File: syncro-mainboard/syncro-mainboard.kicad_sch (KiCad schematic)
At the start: 0 parts

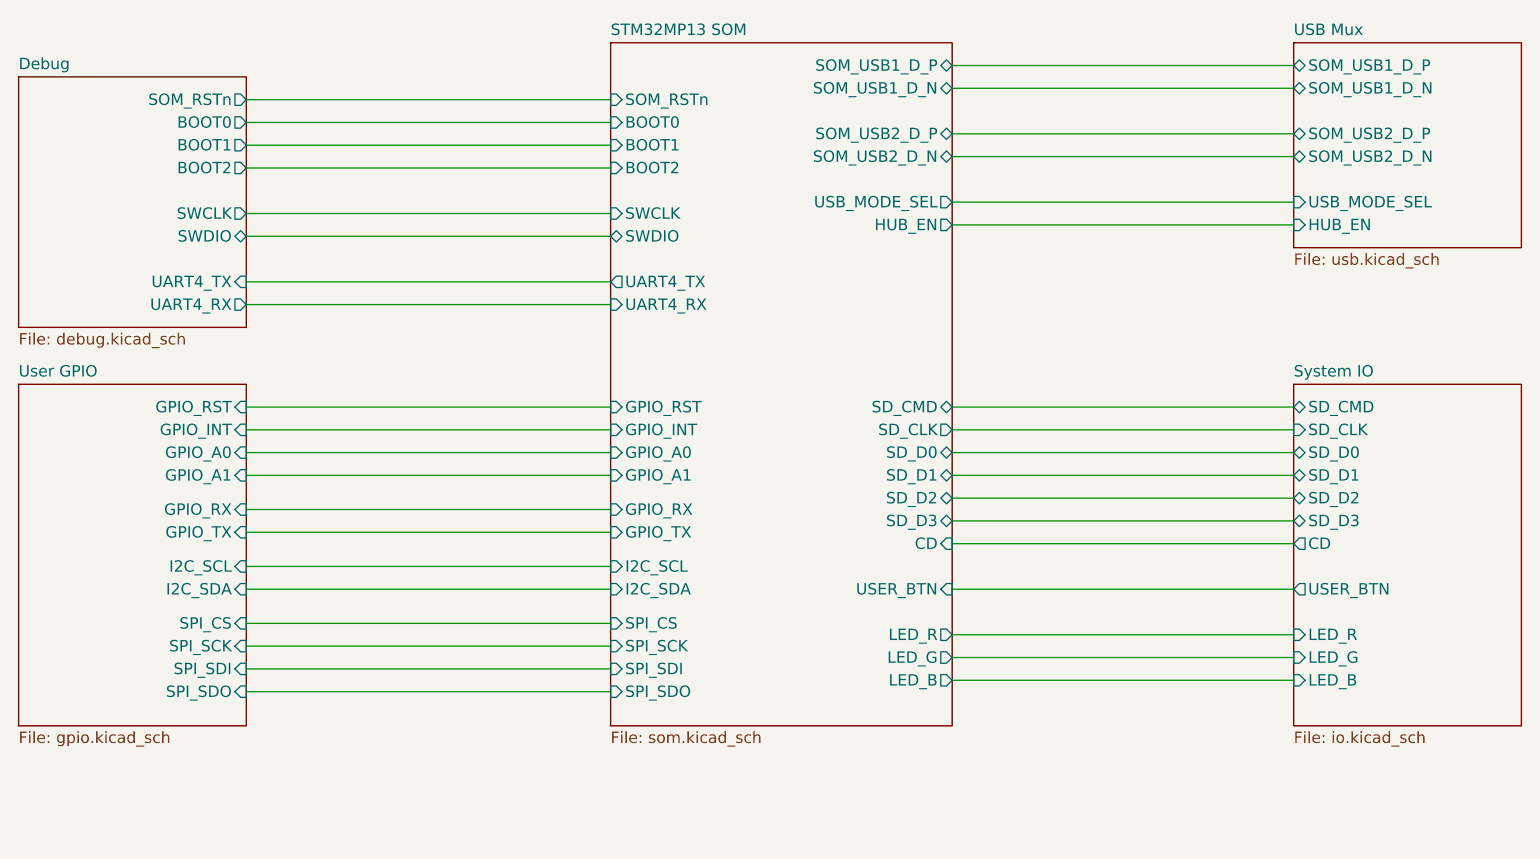
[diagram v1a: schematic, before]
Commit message: Syncro mainboard rev 3
* Add XL-1615 accent RGB LEDs D16-D18 on TIM8
* Add R48-R56 next to the LEDs and rework their shared +3.3V feed
* Add In2 GND return plane under the USB-C connector for TP5/TP6
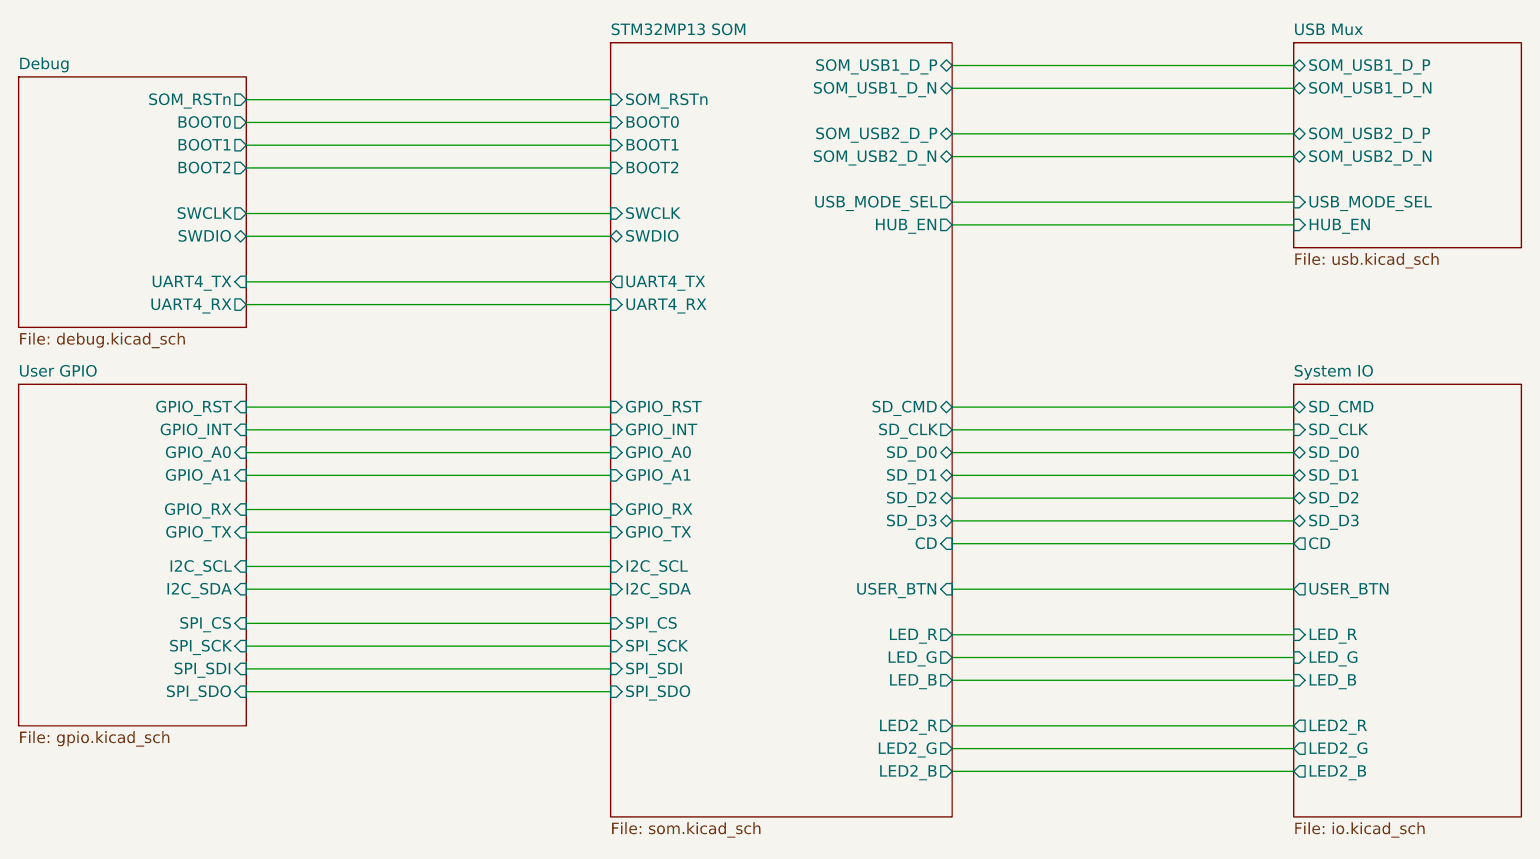
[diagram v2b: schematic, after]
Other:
- sheet STM32MP13 SOM ports: added LED2_B, LED2_G, LED2_R; removed none
- sheet System IO ports: added LED2_B, LED2_G, LED2_R; removed none
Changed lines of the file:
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@@
+	(wire
+		(pts
+			(xy 154.94 143.51) (xy 193.04 143.51)
+		)
+		(stroke
+			(width 0)
+			(type default)
+		)
+	)
 	(wire
 		(pts
@@
 	(wire
 		(pts
+			(xy 154.94 140.97) (xy 193.04 140.97)
+		)
+		(stroke
+			(width 0)
+			(type default)
+		)
+	)
+	(wire
+		(pts
 			(xy 154.94 128.27) (xy 193.04 128.27)
 		)
@@
 		(pts
 			(xy 154.94 107.95) (xy 193.04 107.95)
+		)
+		(stroke
+			(width 0)
+			(type default)
+		)
+	)
+	(wire
+		(pts
+			(xy 154.94 138.43) (xy 193.04 138.43)
 		)
 		(stroke
@@
 	(sheet
 		(at 116.84 62.23)
-		(size 38.1 76.2)
+		(size 38.1 86.36)
 		(exclude_from_sim no)
 		(in_bom yes)
@@
 		)
 		(property "Sheetfile" "som.kicad_sch"
-			(at 116.84 139.0146 0)
+			(at 116.84 149.1746 0)
 			(show_name no)
 			(do_not_autoplace no)
@@
 				)
 				(justify left)
+			)
+		)
+		(pin "LED2_B" output
+			(at 154.94 143.51 0)
+			(effects
+				(font
+					(size 1.27 1.27)
+				)
+				(justify right)
+			)
+		)
+		(pin "LED2_G" output
+			(at 154.94 140.97 0)
+			(effects
+				(font
+					(size 1.27 1.27)
+				)
+				(justify right)
+			)
+		)
+		(pin "LED2_R" output
+			(at 154.94 138.43 0)
+			(effects
+				(font
+					(size 1.27 1.27)
+				)
+				(justify right)
 			)
 		)
@@
 	(sheet
 		(at 193.04 100.33)
-		(size 25.4 38.1)
+		(size 25.4 48.26)
 		(exclude_from_sim no)
 		(in_bom yes)
@@
 		)
 		(property "Sheetfile" "io.kicad_sch"
-			(at 193.04 139.0146 0)
+			(at 193.04 149.1746 0)
 			(show_name no)
 			(do_not_autoplace no)
@@
 			(effects
 				(font
+					(size 1.27 1.27)
+				)
+				(justify left)
+			)
+		)
+		(pin "LED2_B" output
+			(at 193.04 143.51 180)
+			(effects
+				(font
+					(size 1.27 1.27)
+				)
+				(justify left)
+			)
+		)
+		(pin "LED2_G" output
+			(at 193.04 140.97 180)
+			(effects
+				(font
+					(size 1.27 1.27)
+				)
+				(justify left)
+			)
+		)
+		(pin "LED2_R" output
+			(at 193.04 138.43 180)
+			(effects
+				(font
